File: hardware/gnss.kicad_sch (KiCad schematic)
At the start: 0 parts

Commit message: Prel. pin assignments for base station
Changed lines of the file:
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@@
+		)
+	)
+	(hierarchical_label "SDA"
+		(shape bidirectional)
+		(at 115.57 92.71 270)
+		(effects
+			(font
+				(size 1.27 1.27)
+			)
+			(justify right)
+		)
+	)
+	(hierarchical_label "RXD"
+		(shape input)
+		(at 133.35 60.96 0)
+		(effects
+			(font
+				(size 1.27 1.27)
+			)
+			(justify left)
+		)
+	)
+	(hierarchical_label "3V3"
+		(shape input)
+		(at 115.57 38.1 90)
+		(effects
+			(font
+				(size 1.27 1.27)
+			)
+			(justify left)
+		)
+	)
+	(hierarchical_label "TXD"
+		(shape input)
+		(at 133.35 64.77 0)
+		(effects
+			(font
+				(size 1.27 1.27)
+			)
+			(justify left)
 		)
 	)
 	(hierarchical_label "GND"
 		(shape input)
-		(at 45.72 59.69 90)
+		(at 119.38 92.71 270)
+		(effects
+			(font
+				(size 1.27 1.27)
+			)
+			(justify right)
+		)
+	)
+	(hierarchical_label "SCL"
+		(shape input)
+		(at 133.35 68.58 0)
 		(effects
 			(font
@@
 	(symbol
 		(lib_id "power:GND")
-		(at 45.72 59.69 0)
+		(at 119.38 92.71 180)
 		(unit 1)
 		(exclude_from_sim no)
@@
 		(fields_autoplaced yes)
 		(property "Reference" "#PWR03"
-			(at 45.72 66.04 0)
+			(at 119.38 86.36 0)
 			(effects
 				(font
@@
 		)
 		(property "Value" "GND"
-			(at 45.72 64.77 0)
+			(at 119.38 87.63 0)
 			(effects
 				(font
@@
 		)
 		(property "Footprint" ""
-			(at 45.72 59.69 0)
+			(at 119.38 92.71 0)
 			(effects
 				(font
@@
 		)
 		(property "Datasheet" ""
-			(at 45.72 59.69 0)
+			(at 119.38 92.71 0)
 			(effects
 				(font
@@
 		)
 		(property "Description" "Power symbol creates a global label with name \"GND\" , ground"
-			(at 45.72 59.69 0)
+			(at 119.38 92.71 0)
 			(effects
 				(font
@@
 					(unit 1)
 				)
+			)
+		)
+	)
+	(symbol
+		(lib_id "power:+3V3")
+		(at 115.57 38.1 180)
+		(unit 1)
+		(exclude_from_sim no)
+		(in_bom yes)
+		(on_board yes)
+		(dnp no)
+		(fields_autoplaced yes)
+		(property "Reference" "#PWR05"
+			(at 115.57 34.29 0)
+			(effects
+				(font
+					(size 1.27 1.27)
+				)
+				(hide yes)
+			)
+		)
+		(property "Value" "+3V3"
+			(at 115.57 43.18 0)
+			(effects
+				(font
+					(size 1.27 1.27)
+				)
+			)
+		)
+		(property "Footprint" ""
+			(at 115.57 38.1 0)
+			(effects
+				(font
+					(size 1.27 1.27)
+				)
+				(hide yes)
+			)
+		)
+		(property "Datasheet" ""
+			(at 115.57 38.1 0)
+			(effects
+				(font
+					(size 1.27 1.27)
+				)
+				(hide yes)
+			)
+		)
+		(property "Description" "Power symbol creates a global label with name \"+3V3\""
+			(at 115.57 38.1 0)
+			(effects
+				(font
+					(size 1.27 1.27)
+				)
+				(hide yes)
+			)
+		)
+		(pin "1"
+		)
+		(instances
+			(project ""
+				(path "/586b9940-aa00-4ed6-8067-85ee77ecee7e/fc20c7e1-88bc-4c2e-9fe8-716eecb20392"
+					(reference "#PWR05")
+					(unit 1)
+				)
+			)
+		)
+	)
+	(symbol
+		(lib_id "power:+3V3")
+		(at 82.55 60.96 270)
+		(unit 1)
+		(exclude_from_sim no)
+		(in_bom yes)
+		(on_board yes)
+		(dnp no)
+		(fields_autoplaced yes)
+		(property "Reference" "#PWR06"
+			(at 78.74 60.96 0)
+			(effects
+				(font
+					(size 1.27 1.27)
+				)
+				(hide yes)
+			)
+		)
+		(property "Value" "+3V3"
+			(at 86.36 60.9599 90)
+			(effects
+				(font
+					(size 1.27 1.27)
+				)
+				(justify left)
+			)
+		)
+		(property "Footprint" ""
+			(at 82.55 60.96 0)
+			(effects
+				(font
+					(size 1.27 1.27)
+				)
+				(hide yes)
+			)
+		)
+		(property "Datasheet" ""
+			(at 82.55 60.96 0)
+			(effects
+				(font
+					(size 1.27 1.27)
+				)
+				(hide yes)
+			)
+		)
+		(property "Description" "Power symbol creates a global label with name \"+3V3\""
+			(at 82.55 60.96 0)
+			(effects
+				(font
+					(size 1.27 1.27)
+				)
+				(hide yes)
+			)
+		)
+		(pin "1"
+		)
+		(instances
+			(project "hardware"
+				(path "/586b9940-aa00-4ed6-8067-85ee77ecee7e/fc20c7e1-88bc-4c2e-9fe8-716eecb20392"
+					(reference "#PWR06")
+					(unit 1)
+				)

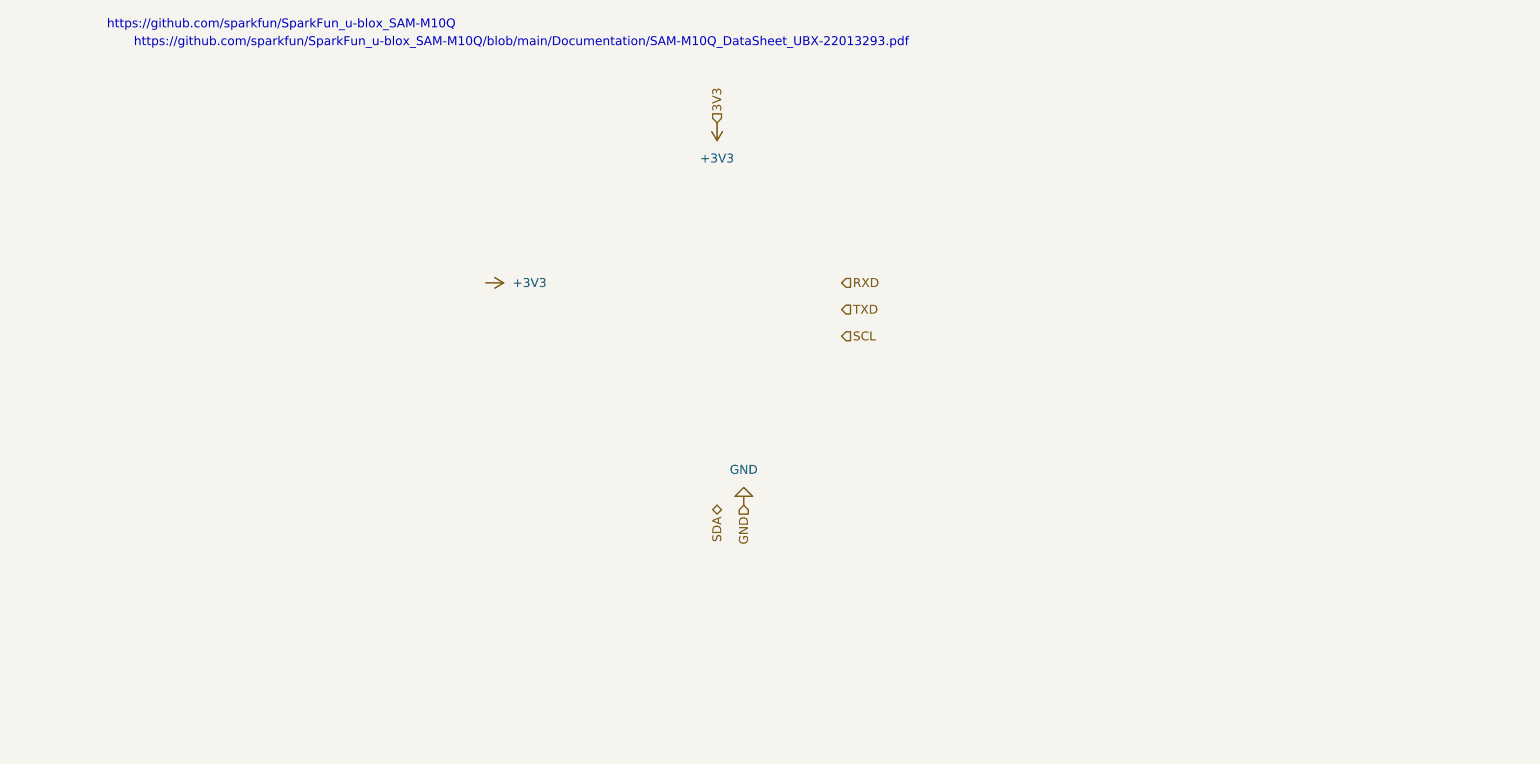
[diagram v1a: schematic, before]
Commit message: added footprints, symbols and so on. also added esp32 to main schematic
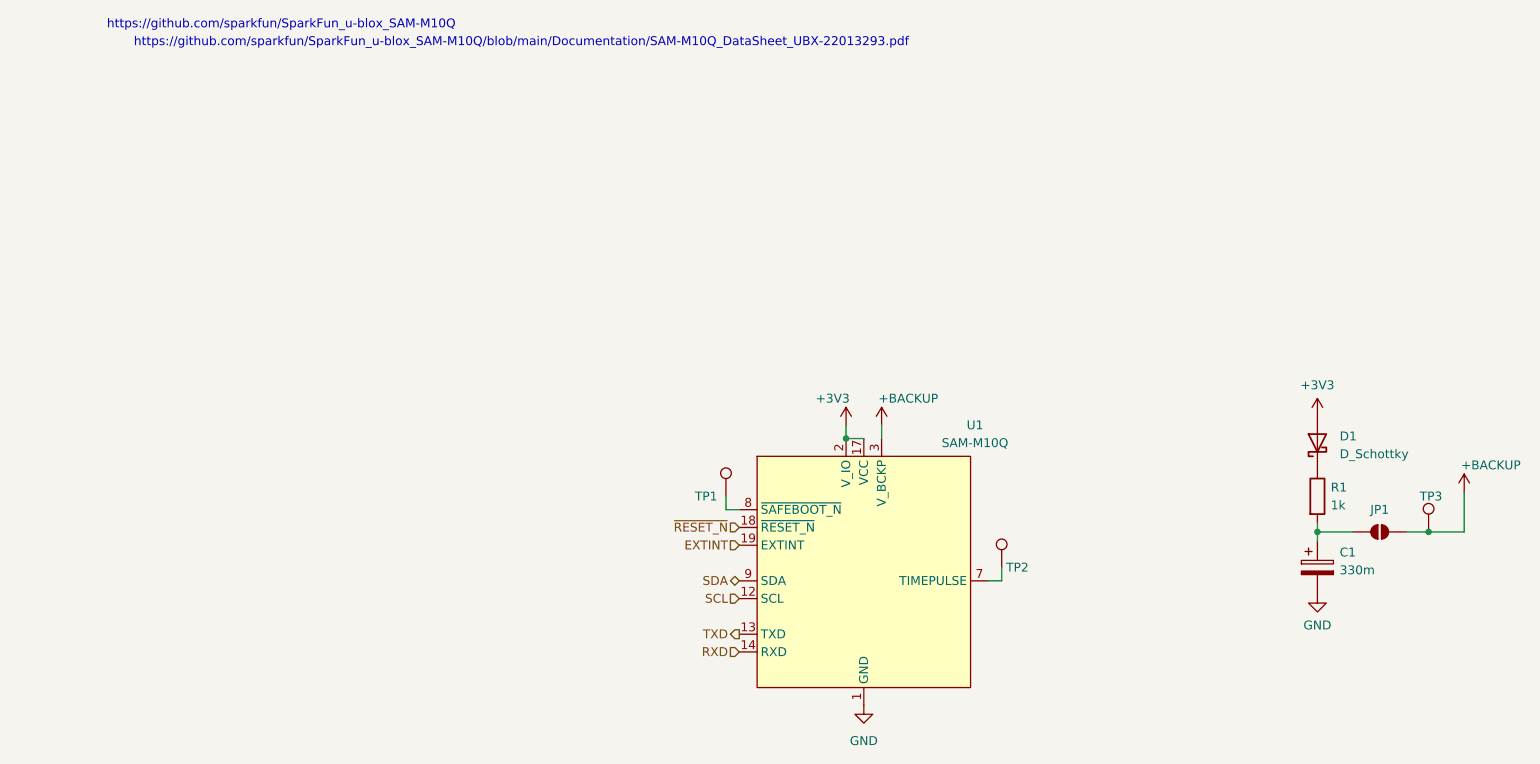
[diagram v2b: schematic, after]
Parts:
- added C1: 330m, symbol Device:C_Polarized
- added D1: D_Schottky, symbol Device:D_Schottky
- added JP1: SolderJumper_2_Open, symbol Jumper:SolderJumper_2_Open
- added R1: 1k, symbol Device:R
- added TP1, TP2, TP3: TestPoint, symbol Connector:TestPoint
- added U1: SAM-M10Q, symbol _symbols:SAM-M10Q
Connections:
- net +3V3: now also D1.2 (A), U1.17 (VCC), U1.2 (V_IO)
- net GND: now also C1.2, U1.1 (GND), U1.10 (GND), U1.11 (GND), U1.15 (GND), U1.16 (GND), U1.20 (GND), U1.4 (GND), U1.5 (GND), U1.6 (GND)
- net RXD: now also U1.14 (RXD)
- net SCL: now also U1.12 (SCL)
- net SDA: now also U1.9 (SDA)
- net TXD: now also U1.13 (TXD)
- new net: TP2.1, U1.7 (TIMEPULSE)
- new net: D1.1 (K), R1.1
- new net: C1.1, JP1.1 (A), R1.2
- new net: TP1.1, U1.8 (~{SAFEBOOT_N})
- new net +BACKUP: JP1.2 (B), TP3.1, U1.3 (V_BCKP)
- new net EXTINT: U1.19 (EXTINT)
- new net ~{RESET_N}: U1.18 (~{RESET_N})
